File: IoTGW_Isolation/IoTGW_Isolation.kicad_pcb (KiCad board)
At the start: 2 copper layers, 7 parts, among them U2 HCPL-0600, U3 TLE2426xD, U4 VO2630, U5 TEA1-0505, U6 ISO1452BDWR, U7 PC817, U8 PC817

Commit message: footprints + pcb
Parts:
- added C1: 100nF, Capacitor_SMD:C_0805_2012Metric_Pad1.18x1.45mm_HandSolder, F.Cu at (139.0, 53.5)
- added C2: 100nF, Capacitor_SMD:C_0805_2012Metric_Pad1.18x1.45mm_HandSolder, F.Cu at (139.0, 56.6)
- added C3: 10uF, Capacitor_Tantalum_SMD:CP_EIA-3216-18_Kemet-A_Pad1.58x1.35mm_HandSolder, F.Cu at (139.7, 59.6)
- added F1: Polyfuse, Fuse:Fuse_0805_2012Metric, F.Cu at (138.8, 62.7)
- added H1: M3, MountingHole:MountingHole_3.2mm_M3_Pad_Via, F.Cu at (118.8, 93.8)
- added H2: M3, MountingHole:MountingHole_3.2mm_M3_Pad_Via, F.Cu at (118.8, 121.2)
- added H3: M3, MountingHole:MountingHole_3.2mm_M3_Pad_Via, F.Cu at (171.2, 93.8)
- added H4: M3, MountingHole:MountingHole_3.2mm_M3_Pad_Via, F.Cu at (171.2, 121.3)
- added J1: Molex 39502-1002, IoTGW:Molex_2pin_3.50, F.Cu at (126.5, 110.5)
- added J3: Molex 39502-1007, IoTGW:Molex_7pin_3.50, F.Cu at (133.1, 124.6)
- added R10: 200R, Resistor_SMD:R_0805_2012Metric_Pad1.20x1.40mm_HandSolder, F.Cu at (129.5, 62.4)
- added R11: 200R, Resistor_SMD:R_0805_2012Metric_Pad1.20x1.40mm_HandSolder, F.Cu at (129.5, 65.3)
- added R12: 10k, Resistor_SMD:R_0805_2012Metric_Pad1.20x1.40mm_HandSolder, F.Cu at (134.3, 53.5)
- added R13: 10k, Resistor_SMD:R_0805_2012Metric_Pad1.20x1.40mm_HandSolder, F.Cu at (134.3, 56.5)
- added R14: 10k, Resistor_SMD:R_0805_2012Metric_Pad1.20x1.40mm_HandSolder, F.Cu at (134.3, 59.4)
- added R2: 120R, Resistor_SMD:R_0805_2012Metric_Pad1.20x1.40mm_HandSolder, F.Cu at (124.8, 53.5)
- added R3: 200R, Resistor_SMD:R_0805_2012Metric_Pad1.20x1.40mm_HandSolder, F.Cu at (124.8, 56.5)
- added R4: 200R, Resistor_SMD:R_0805_2012Metric_Pad1.20x1.40mm_HandSolder, F.Cu at (124.8, 59.4)
- added R5: 200R, Resistor_SMD:R_0805_2012Metric_Pad1.20x1.40mm_HandSolder, F.Cu at (124.8, 62.4)
- added R6: 10k, Resistor_SMD:R_0805_2012Metric_Pad1.20x1.40mm_HandSolder, F.Cu at (124.8, 65.3)
- added R7: 10k, Resistor_SMD:R_0805_2012Metric_Pad1.20x1.40mm_HandSolder, F.Cu at (129.5, 53.5)
- added R8: 10k, Resistor_SMD:R_0805_2012Metric_Pad1.20x1.40mm_HandSolder, F.Cu at (129.5, 56.5)
- added R9: 200R, Resistor_SMD:R_0805_2012Metric_Pad1.20x1.40mm_HandSolder, F.Cu at (129.5, 59.4)
- added U1: TEA1-0505, Converter_DCDC:Converter_DCDC_TRACO_TEA1-xxxx_THT, F.Cu at (157.4, 97.0)
- U2: value HCPL-0600 -> ISO1452BDWR; footprint Package_SO:SOIC-8_3.9x4.9mm_P1.27mm -> Package_SO:SOIC-16W_7.5x10.3mm_P1.27mm
- U3: value TLE2426xD -> LTV-817S; footprint Package_SO:SOIC-8_3.9x4.9mm_P1.27mm -> Package_DIP:SMDIP-4_W9.53mm; moved to B.Cu
- U4: value VO2630 -> LTV-817S; footprint Package_DIP:DIP-8_W7.62mm -> Package_DIP:SMDIP-4_W9.53mm; moved to B.Cu
- U5: value TEA1-0505 -> LTV-817S; footprint Converter_DCDC:Converter_DCDC_TRACO_TEA1-xxxx_THT -> Package_DIP:SMDIP-4_W9.53mm; moved to B.Cu
- U6: value ISO1452BDWR -> LTV-817S; footprint Package_SO:SOIC-16W_7.5x10.3mm_P1.27mm -> Package_DIP:SMDIP-4_W9.53mm; moved to B.Cu
- U7, U8: value PC817 -> LTV-817S; footprint Package_DIP:DIP-4_W7.62mm -> Package_DIP:SMDIP-4_W9.53mm; moved to B.Cu
- moved U6 44.6 mm to (101.0, 84.2), turned to 180 degrees
- moved U2 35.8 mm to (146.8, 103.0)
- moved U3 34.8 mm to (101.0, 64.2), turned to 180 degrees
- moved U7 29.5 mm to (101.0, 90.8), turned to 180 degrees
- moved U8 29.4 mm to (101.0, 97.5), turned to 180 degrees
- moved U4 22.1 mm to (101.0, 70.9), turned to 180 degrees
- moved U5 14.2 mm to (101.0, 77.5), turned to 180 degrees
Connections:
- U2 pad 1: unconnected-(U2-NC-Pad1) -> +5V
- U2 pad 2: Net-(U2-A) -> GND
- U2 pad 3: GND -> GPIO_R
- U2 pad 4: (no net) -> GPIO_~{RE}
- U2 pad 5: GND_OUT -> GPIO_DE
- U2 pad 6: unconnected-(U2-VO-Pad6) -> GPIO_D
- U2 pad 8: unconnected-(U2-VCC-Pad8) -> GND
- U3 pad 1: GND1 -> Net-(R3-Pad1)
- U3 pad 3: VCC -> GND_OUT
- U3 pad 4: unconnected-(U3-NC-Pad4) -> GPIO_EXT_0
- U4 pad 1: unconnected-(U4-A1-Pad1) -> Net-(R4-Pad1)
- U4 pad 2: unconnected-(U4-C1-Pad2) -> GND
- U4 pad 3: unconnected-(U4-C2-Pad3) -> GND_OUT
- U4 pad 4: unconnected-(U4-A2-Pad4) -> GPIO_EXT_1
- U5 pad 1: GND -> Net-(R5-Pad1)
- U5 pad 2: +5V -> GND
- U5 pad 4: +5V_OUT -> GPIO_EXT_2
- U6 pad 1: +5V -> Net-(R9-Pad1)
- U6 pad 2: GND -> GND_OUT
- U6 pad 3: GPIO_ -> GND
- U6 pad 4: GPIO_~{RE} -> GPIO_OPTO_0
- U7 pad 2: GND -> GND_OUT
- U7 pad 3: GND_OUT -> GND
- U7 pad 4: GPIO_EXT_0 -> GPIO_OPTO_1
- U8 pad 4: GPIO_0 -> GPIO_OPTO_2
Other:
- board outline added: 60 x 35 mm
- copper layers 2 -> 4

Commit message: PCB update, connectors 8pin
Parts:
- removed J1: Molex 39502-1002, IoTGW:Molex_2pin_3.50
- removed J3: Molex 39502-1007, IoTGW:Molex_7pin_3.50
- added J4: 39502-1008, IoTGW:Molex_8pin_3.50, F.Cu at (115.2, 97.8)
- added J5: 39502-1008, IoTGW:Molex_8pin_3.50, F.Cu at (174.8, 127.2)
- moved F1 66.8 mm to (163.5, 124.8)
- moved R11 46.8 mm to (154.5, 104.9)
- moved R6 46.8 mm to (149.8, 104.9)
- moved C2 46.8 mm to (164.0, 96.1)
- moved R10 46.8 mm to (154.5, 102.0)
- moved R14 46.8 mm to (159.2, 99.0)
- moved R4 46.8 mm to (149.8, 99.0)
- moved R5 46.8 mm to (149.8, 102.0)
- moved R9 46.8 mm to (154.5, 99.0)
- moved C1 46.8 mm to (164.0, 93.1)
- moved R12 46.8 mm to (159.2, 93.1)
- moved R13 46.8 mm to (159.2, 96.0)
- moved R2 46.8 mm to (149.8, 93.1)
- moved R3 46.8 mm to (149.8, 96.0)
- moved R7 46.8 mm to (154.5, 93.1)
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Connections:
- U2 pad 4: GPIO_~{RE} -> GPIO_COMM
- U2 pad 5: GPIO_DE -> GPIO_COMM
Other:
- board size 60 x 35 mm -> 60 x 45 mm

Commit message: PCB update
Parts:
- removed J5: 39502-1008, IoTGW:Molex_8pin_3.50
- added J1: 39502-1008, IoTGW:Molex_8pin_3.50, F.Cu at (174.9, 127.2)
- moved C2 28.2 mm to (138.0, 107.0), turned to 90 degrees
- moved R3 24.4 mm to (141.5, 119.0), turned to 180 degrees
- moved F1 24.4 mm to (161.0, 100.5)
- moved U5 23.8 mm to (145.0, 128.5), turned to 0 degrees
- moved R12 23.6 mm to (136.2, 98.5), turned to 180 degrees
- moved R4 23.5 mm to (141.5, 121.0), turned to 180 degrees
- moved R13 23.4 mm to (136.2, 100.5), turned to 180 degrees
- moved R14 23.3 mm to (136.2, 102.5), turned to 180 degrees
- moved R5 22.6 mm to (141.5, 123.0), turned to 180 degrees
- moved R9 20.8 mm to (148.8, 119.0)
- moved U6 20.4 mm to (145.0, 99.8)
- moved U4 20.0 mm to (145.0, 117.0), turned to 0 degrees
- moved R10 19.9 mm to (148.8, 121.0)
- moved R11 19.0 mm to (148.8, 123.0)
- moved C1 18.4 mm to (152.0, 107.0), turned to 90 degrees
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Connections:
- C1 pad 1: +5V_PROT -> +5V_OUT
- C3 pad 1: +5V_PROT -> +5V_OUT
- J4 pad 6: GPIO_COMM -> GPIO_R
- J4 pad 7: GPIO_R -> GPIO_COMM
- R12 pad 2: +5V_PROT -> +5V
- R13 pad 2: +5V_PROT -> +5V
- R14 pad 2: +5V_PROT -> +5V
- R6 pad 2: +5V_PROT -> +5V_OUT
- R7 pad 2: +5V_PROT -> +5V_OUT
- R8 pad 2: +5V_PROT -> +5V_OUT
- U2 pad 16: +5V_PROT -> +5V_OUT
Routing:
- net +5V: track 0.00 -> 51.6 mm
- net GPIO_EXT_2: track 0.00 -> 46.6 mm, vias 0 -> 2
- net +5V_OUT: track 0.00 -> 34.2 mm
- net GPIO_COMM: track 0.00 -> 22.2 mm
- net GPIO_D: track 0.00 -> 21.7 mm
- net GPIO_OPTO_2: track 0.00 -> 21.6 mm, vias 0 -> 2
- net Net-(R9-Pad1): track 0.00 -> 21.5 mm, vias 0 -> 1
- net RS-485_B: track 0.00 -> 21.2 mm
- net GPIO_R: track 0.00 -> 20.3 mm
- net RS-485_A: track 0.00 -> 20.3 mm
- net GPIO_EXT_1: track 0.00 -> 19.0 mm, vias 0 -> 1
- net Net-(R3-Pad1): track 0.00 -> 13.2 mm, vias 0 -> 1
- net Net-(R10-Pad1): track 0.00 -> 11.9 mm, vias 0 -> 1
- net GPIO_OPTO_1: track 0.00 -> 10.5 mm, vias 0 -> 1
- net GPIO_EXT_0: track 0.00 -> 9.20 mm, vias 0 -> 1
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- added copper zone on B.Cu, net GND
- added copper zone on F.Cu, net GND
- added copper zone on B.Cu, net GND_OUT
- added copper zone on F.Cu, net GND_OUT

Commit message: PCB routing update
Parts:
- moved F1 1.50 mm to (159.5, 100.5)
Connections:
- net RS-485_A renamed RS-485_+
- net RS-485_B renamed RS-485_-
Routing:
- net GPIO_OPTO_0: track 2.49 -> 43.2 mm, vias 1 -> 3
- net GPIO_OPTO_1: track 10.5 -> 51.3 mm, vias 1 -> 3
- net GPIO_EXT_0: track 9.20 -> 43.9 mm, vias 1 -> 2
- net GPIO_EXT_1: track 19.0 -> 44.6 mm, vias 1 -> 3
- net GPIO_OPTO_2: track 21.6 -> 42.6 mm
- net GND_OUT: track 0.00 -> 4.68 mm, vias 0 -> 63
- net 5V_CONN: track 5.29 -> 6.79 mm
- net +5V_OUT: track 34.2 -> 32.7 mm
- net GPIO_COMM: track 22.2 -> 23.4 mm
- net GND: track 0.00 -> 0.99 mm, vias 0 -> 51
- net GPIO_EXT_2: track 46.6 -> 47.4 mm
- net RS-485_-: track 21.2 -> 21.9 mm

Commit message: pcb updates schemartic update
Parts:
- added TP1: LOGO, IoTGW:INSET_LOGO, F.Cu at (134.0, 130.0)
- moved J1 0.07 mm to (174.8, 127.2)
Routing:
- net GND_OUT: track 4.68 -> 10.8 mm, vias 63 -> 78
- net GND: track 0.99 -> 4.13 mm, vias 51 -> 68
- net GPIO_EXT_2: track 47.4 -> 48.1 mm
- net Net-(R4-Pad1): track 3.69 -> 4.36 mm
- net GPIO_OPTO_2: track 42.6 -> 43.1 mm
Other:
- board text added: "5V"
- board text added: "GND"
- board text added: "IO_0"
- board text added: "IO_1"
- board text added: "IO_2"
- board text added: "MD"
- board text added: "NC"
- board text added: "RSA"
- board text added: "RSB"
- board text added: "RX"
- board text added: "TX"

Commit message: pdfs
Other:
- board text added: "M3"

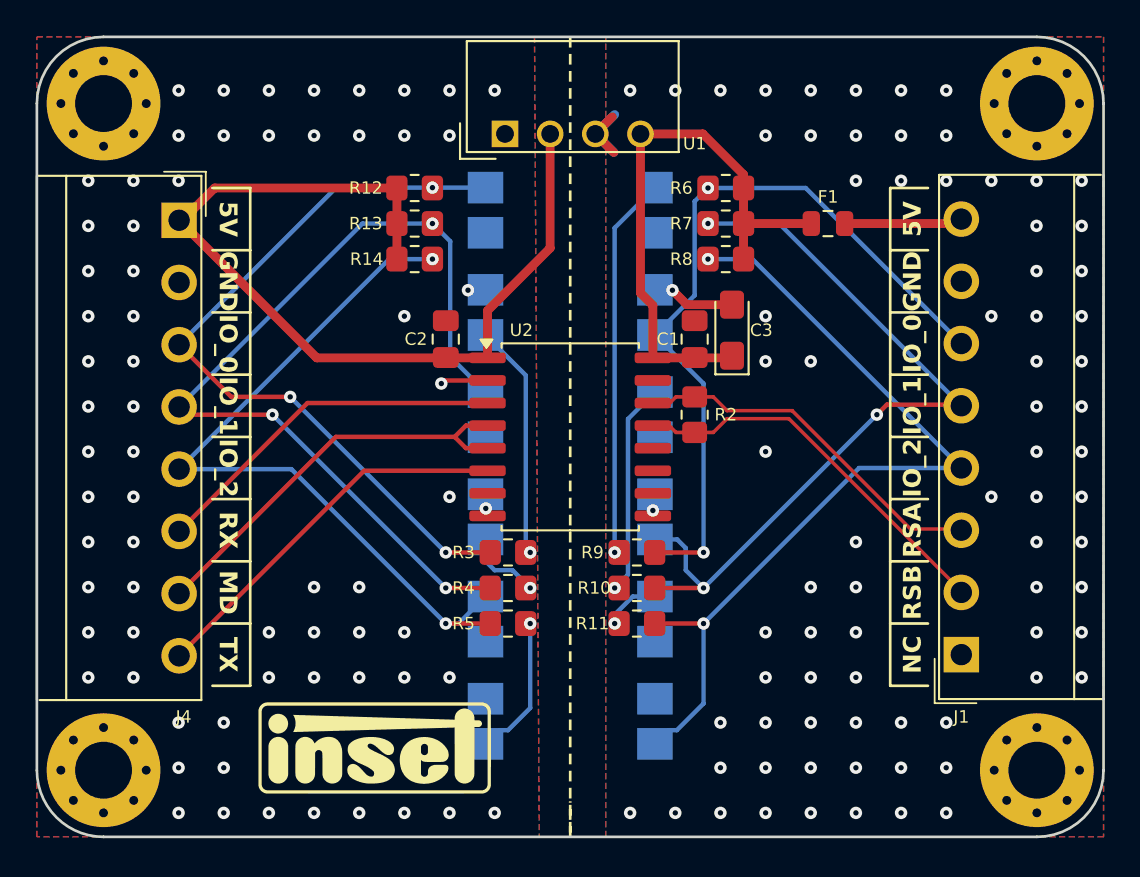
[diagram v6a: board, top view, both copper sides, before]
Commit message: smaller PCB
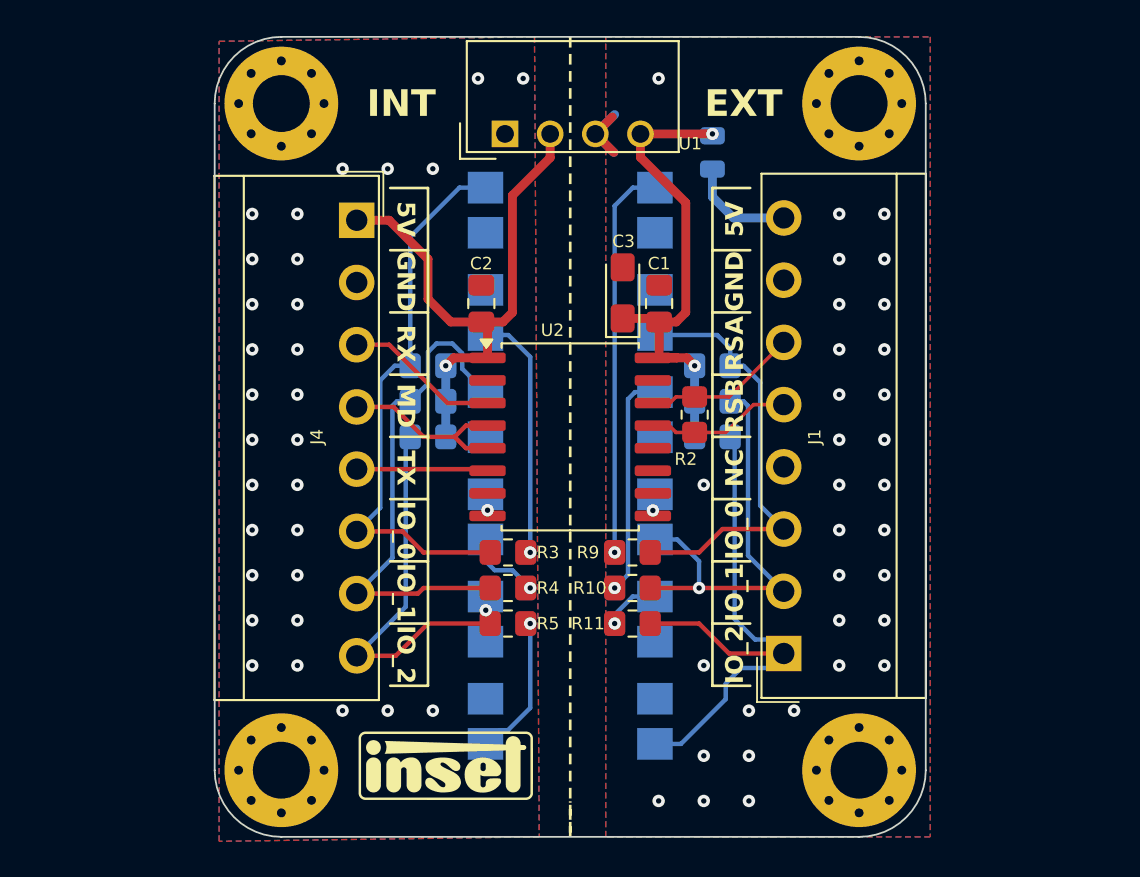
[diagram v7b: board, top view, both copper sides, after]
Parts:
- F1, R12, R13, R14, R6, R7, R8: moved to B.Cu
- moved R12 10.0 mm to (137.0, 108.5), turned to 0 degrees
- moved R13 10.0 mm to (137.0, 110.5), turned to 0 degrees
- moved R14 10.0 mm to (137.0, 112.5), turned to 0 degrees
- moved R6 10.0 mm to (153.0, 108.5), turned to 180 degrees
- moved R7 10.0 mm to (153.0, 110.5), turned to 180 degrees
- moved R8 10.0 mm to (153.0, 112.5), turned to 180 degrees
- moved H1 10.0 mm to (128.8, 93.8)
- moved H3 10.0 mm to (161.2, 93.8)
- moved H2 10.00 mm to (128.8, 131.2)
- moved H4 10.00 mm to (161.2, 131.2)
- moved J1 9.99 mm to (164.9, 127.2)
- moved J4 9.99 mm to (125.1, 97.8)
- moved F1 7.63 mm to (153.0, 96.5), turned to -90 degrees
- moved C3 6.50 mm to (147.9, 104.4)
- moved TP1 4.12 mm to (138.0, 131.0)
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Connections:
- J1 pad 1: unconnected-(J1-Pin_1-Pad1) -> GPIO_EXT_2
- J1 pad 2: RS-485_- -> GPIO_EXT_1
- J1 pad 3: RS-485_+ -> GPIO_EXT_0
- J1 pad 4: GPIO_EXT_2 -> unconnected-(J1-Pin_4-Pad4)
- J1 pad 5: GPIO_EXT_1 -> RS-485_-
- J1 pad 6: GPIO_EXT_0 -> RS-485_+
- J4 pad 3: GPIO_OPTO_0 -> GPIO_R
- J4 pad 4: GPIO_OPTO_1 -> GPIO_COMM
- J4 pad 5: GPIO_OPTO_2 -> GPIO_D
- J4 pad 6: GPIO_R -> GPIO_OPTO_0
- J4 pad 7: GPIO_COMM -> GPIO_OPTO_1
- J4 pad 8: GPIO_D -> GPIO_OPTO_2
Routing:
- net GPIO_OPTO_1: track 51.0 -> 28.6 mm, vias 3 -> 0
- net GPIO_OPTO_2: track 43.1 -> 22.3 mm, vias 2 -> 1
- net GPIO_EXT_1: track 44.6 -> 24.2 mm, vias 3 -> 1
- net +5V: track 51.6 -> 32.3 mm, vias 0 -> 1
- net GPIO_EXT_0: track 43.5 -> 24.2 mm, vias 2 -> 0
- net GPIO_EXT_2: track 48.1 -> 32.0 mm, vias 2 -> 0
- net GPIO_D: track 21.7 -> 7.15 mm
- net RS-485_-: track 21.9 -> 8.17 mm
- net GPIO_COMM: track 23.4 -> 10.4 mm
- net RS-485_+: track 20.6 -> 8.77 mm
- net GPIO_OPTO_0: track 43.2 -> 31.5 mm, vias 3 -> 0
- net GPIO_R: track 20.3 -> 8.72 mm
- net GND_OUT: track 10.8 -> 6.15 mm, vias 78 -> 33
- net +5V_OUT: track 32.7 -> 28.6 mm, vias 0 -> 2
- net GND: track 4.13 -> 0.32 mm, vias 68 -> 31
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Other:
- board size 60 x 45 mm -> 40 x 45 mm
- board text added: "0.0900 mm / 0.0900 mm"
- board text added: "0.1000 mm"
- board text added: "1.6000 mm"
- board text added: "2"
- board text added: "40.0000 mm x 45.0000 mm"
- board text added: "BOARD CHARACTERISTICS"
- board text added: "Board Thickness:"
- board text added: "Board overall dimensions:"
- board text added: "Castellated pads:"
- board text added: "Copper Finish:"
- board text added: "Copper Layer Count:"
- board text added: "EXT"
- board text added: "Edge card connectors:"
- board text added: "INT"
- board text added: "Impedance Control:"
- board text added: "Min hole diameter:"
- board text added: "Min track/spacing:"
- board text added: "No"
- board text added: "None"
- board text added: "Plated Board Edge:"

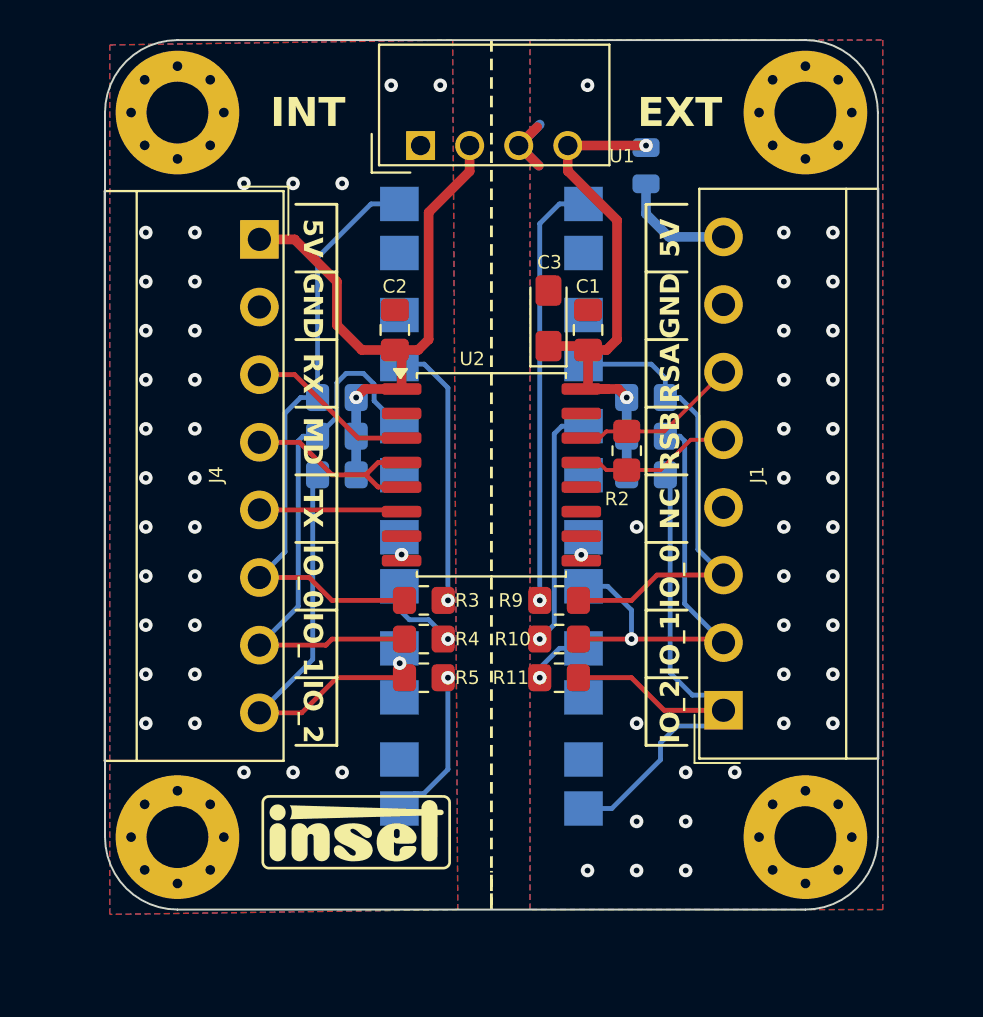
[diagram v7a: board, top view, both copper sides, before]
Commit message: schematic update 3.3V logic
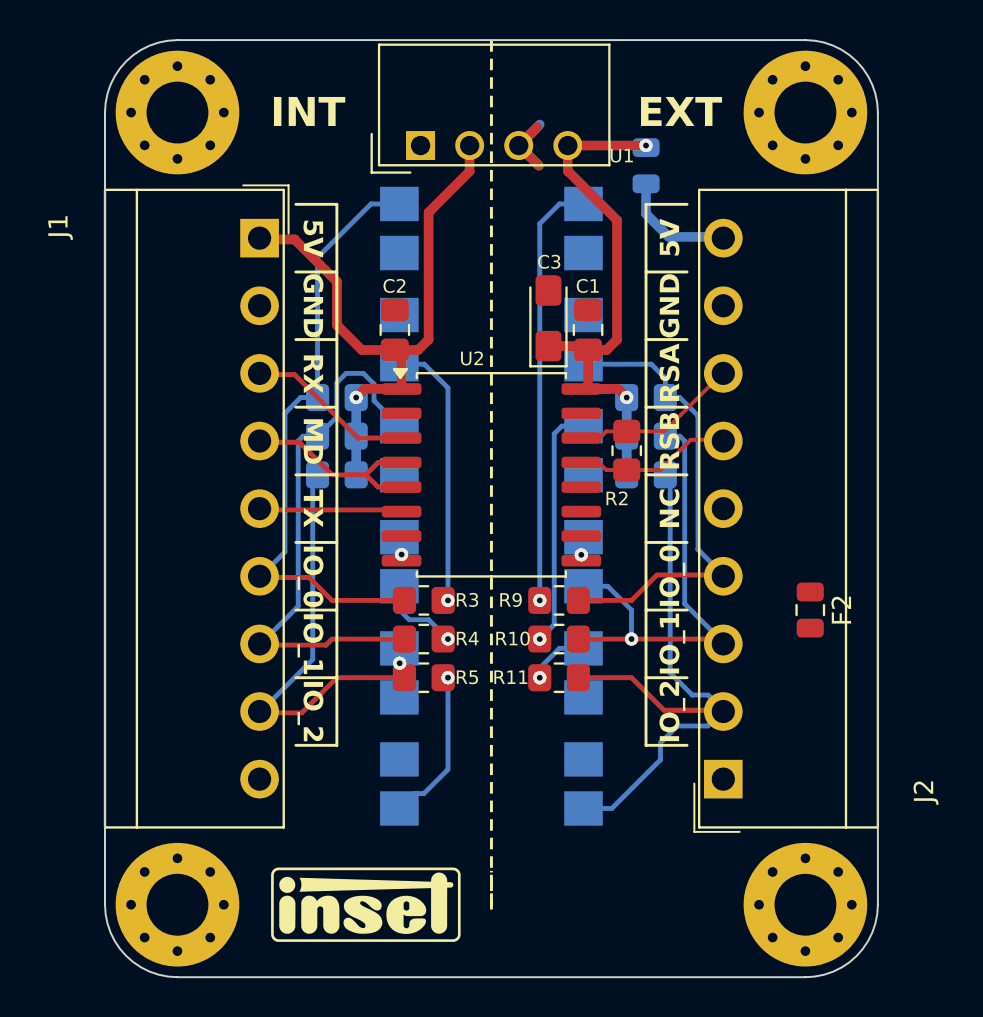
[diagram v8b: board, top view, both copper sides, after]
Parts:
- removed J4: 39502-1008, IoTGW:Molex_8pin_3.50
- added F2: Polyfuse, Fuse:Fuse_0805_2012Metric, F.Cu at (161.5, 119.5)
- added J2: 39502-1009, IoTGW:Molex_9pin_3.50, F.Cu at (164.8, 130.7)
- J1: value 39502-1008 -> 39502-1009; footprint IoTGW:Molex_8pin_3.50 -> IoTGW:Molex_9pin_3.50
- moved J1 49.4 mm to (125.2, 97.8), turned to -90 degrees
- moved TP1 3.78 mm to (138.5, 134.8)
- moved H2 3.50 mm to (128.8, 134.8)
- moved H4 3.50 mm to (161.2, 134.8)
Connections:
- J1 pad 1: GPIO_EXT_2 -> +3.3V
- J1 pad 2: GPIO_EXT_1 -> +5V
- J1 pad 3: GPIO_EXT_0 -> GND
- J1 pad 4: unconnected-(J1-Pin_4-Pad4) -> GPIO_R
- J1 pad 5: RS-485_- -> GPIO_COMM
- J1 pad 6: RS-485_+ -> GPIO_D
- J1 pad 7: GND_OUT -> GPIO_OPTO_0
- J1 pad 8: 5V_CONN -> GPIO_OPTO_1
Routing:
- net GND_OUT: vias 33 -> 1
- net GND: vias 31 -> 1
- removed copper zone on B.Cu, net GND
- removed copper zone on F.Cu, net GND
- removed copper zone on B.Cu, net GND_OUT
- removed copper zone on F.Cu, net GND_OUT
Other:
- board size 40 x 45 mm -> 40 x 48.5 mm
- board text removed: "M3"
